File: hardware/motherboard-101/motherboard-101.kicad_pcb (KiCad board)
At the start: 2 copper layers, 216 x 150 mm, 124 parts, among them J1 PWR_conn, J2 DB25M, J3 MSX_Slot, J4 MSX_Slot, J5 GFX_Connector_Output, J6 CONN_JOY, J7 CONN_JOY, J8 DIN8, K1 Relay, Q1 2N2222, Q2 2N2907, SW1 Push_button, U1 62256, U10 74HC04, U11 74HC32, U12 74HC32, U13 74HC32, U14 74HC08, U15 74HC139, U16 74LS07, U17 74HC74, U18 74HCT08, U19 LM311, U2 62256, U20 SST39SF0, U21 74HC138, U22 74HC138, U23 74HC157, U24 AY-3-8910, U25 74HC157, U26 74HC138, U27 74HC153, U28 82C55A, U3 74HCT244, U4 74HCT244, U5 74HCT244, U6 Z84C00, U7 74HC74, U8 74HCT245, U9 74HCU04, Y1 3.58Mhz

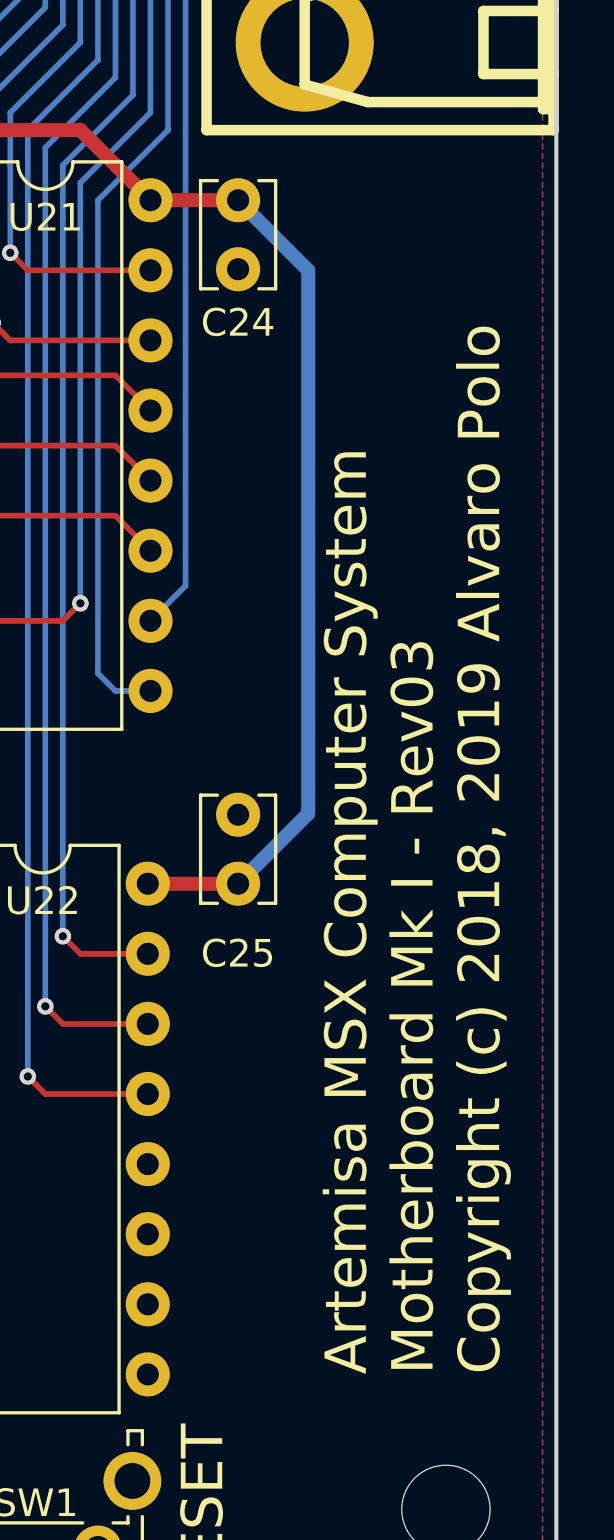
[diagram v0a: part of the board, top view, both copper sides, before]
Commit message: Rename motherboard project to model 101
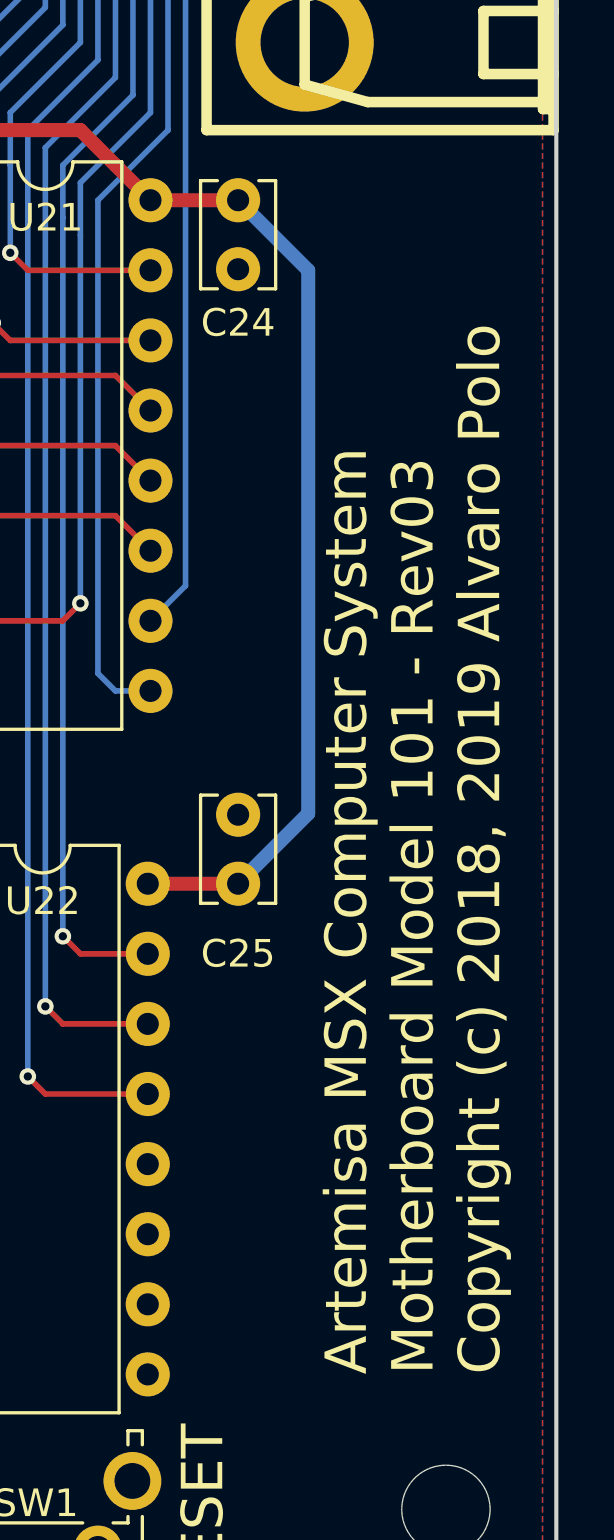
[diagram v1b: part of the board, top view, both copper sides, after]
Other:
- board text added: "Artemisa MSX Computer System Motherboard Model 101 - Rev03 Copyright (c) 2018, 2019 Alvaro Polo"
- board text removed: "Artemisa MSX Computer System Motherboard Mk I - Rev03 Copyright (c) 2018, 2019 Alvaro Polo"
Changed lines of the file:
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@@
     (effects (font (size 1 1) (thickness 0.15)) (justify right))
   )
-  (gr_text "Artemisa MSX Computer System\nMotherboard Mk I - Rev03\nCopyright (c) 2018, 2019 Alvaro Polo" (at 267.716 219.71 90) (layer F.SilkS)
+  (gr_text "Artemisa MSX Computer System\nMotherboard Model 101 - Rev03\nCopyright (c) 2018, 2019 Alvaro Polo" (at 267.716 219.71 90) (layer F.SilkS)
     (effects (font (size 1.5 1.5) (thickness 0.3)) (justify left))
   )
